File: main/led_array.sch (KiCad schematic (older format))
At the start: 220 parts

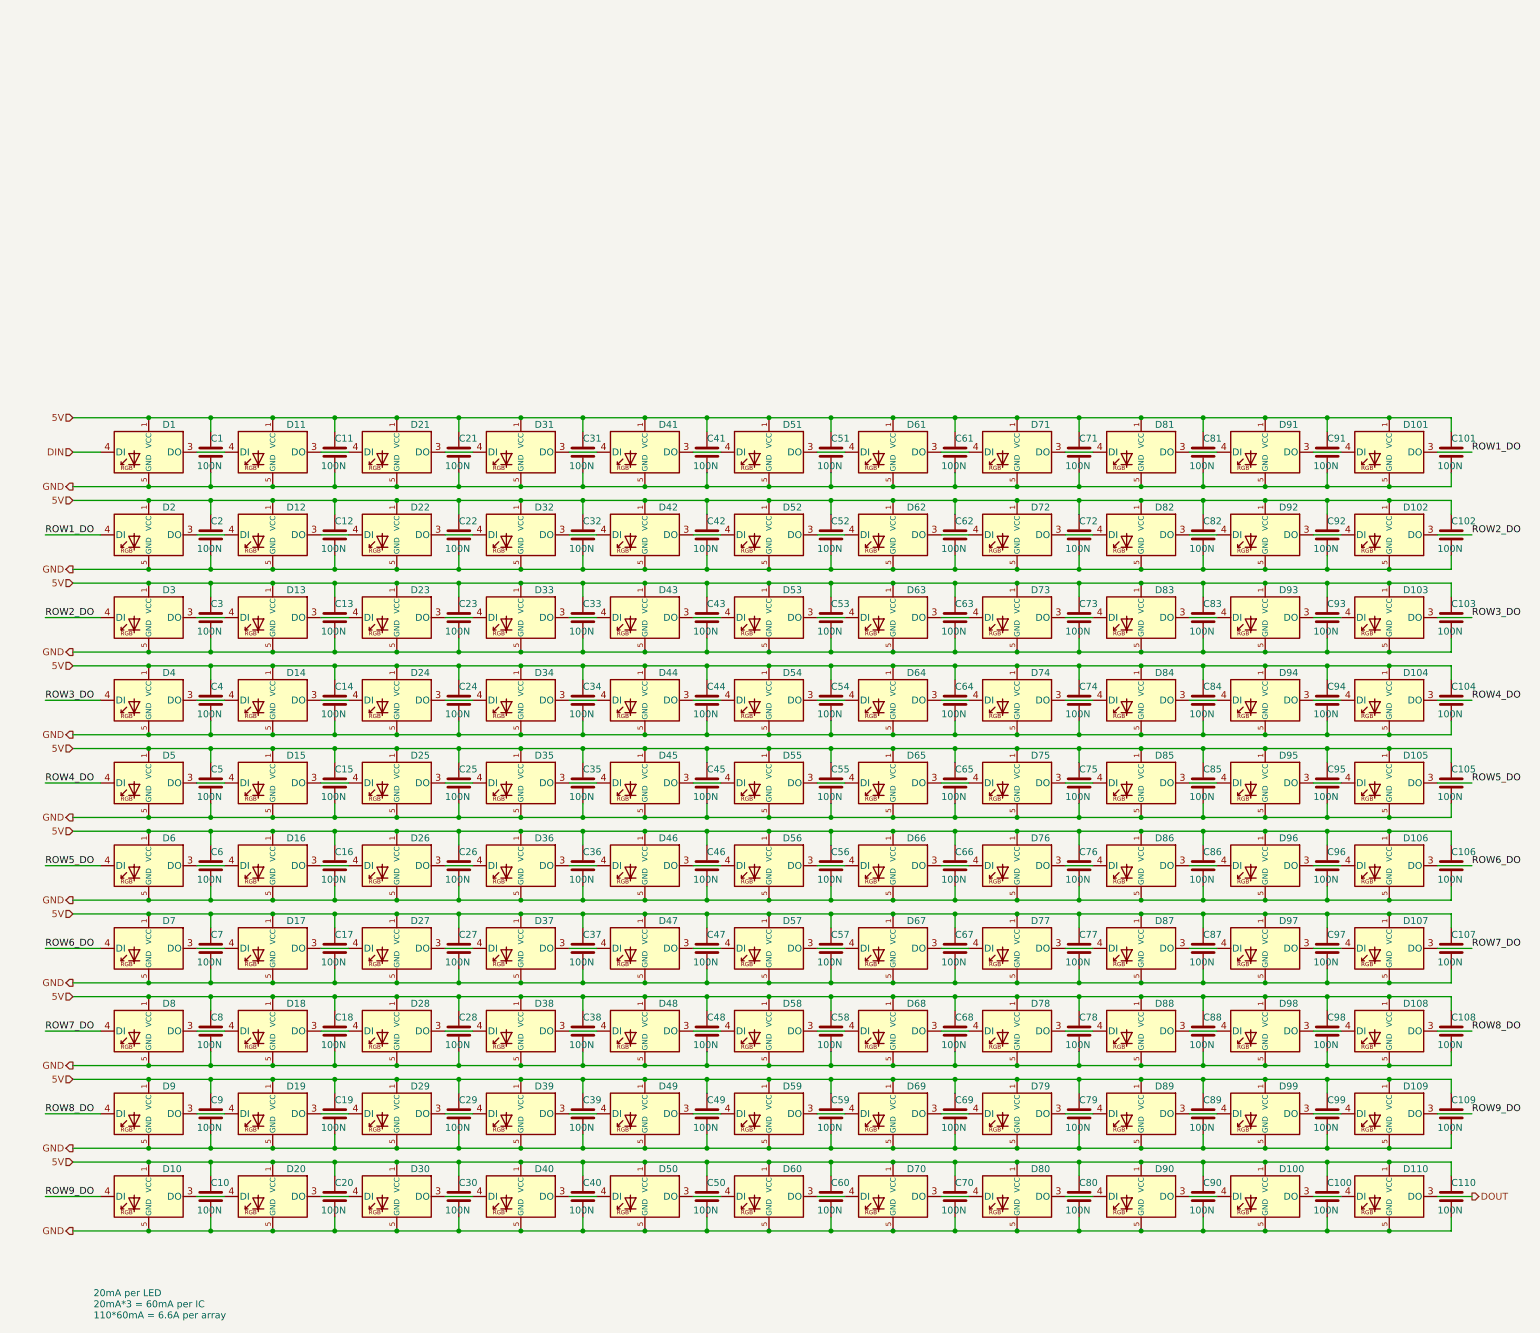
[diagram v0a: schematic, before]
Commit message: started layout to see if practical
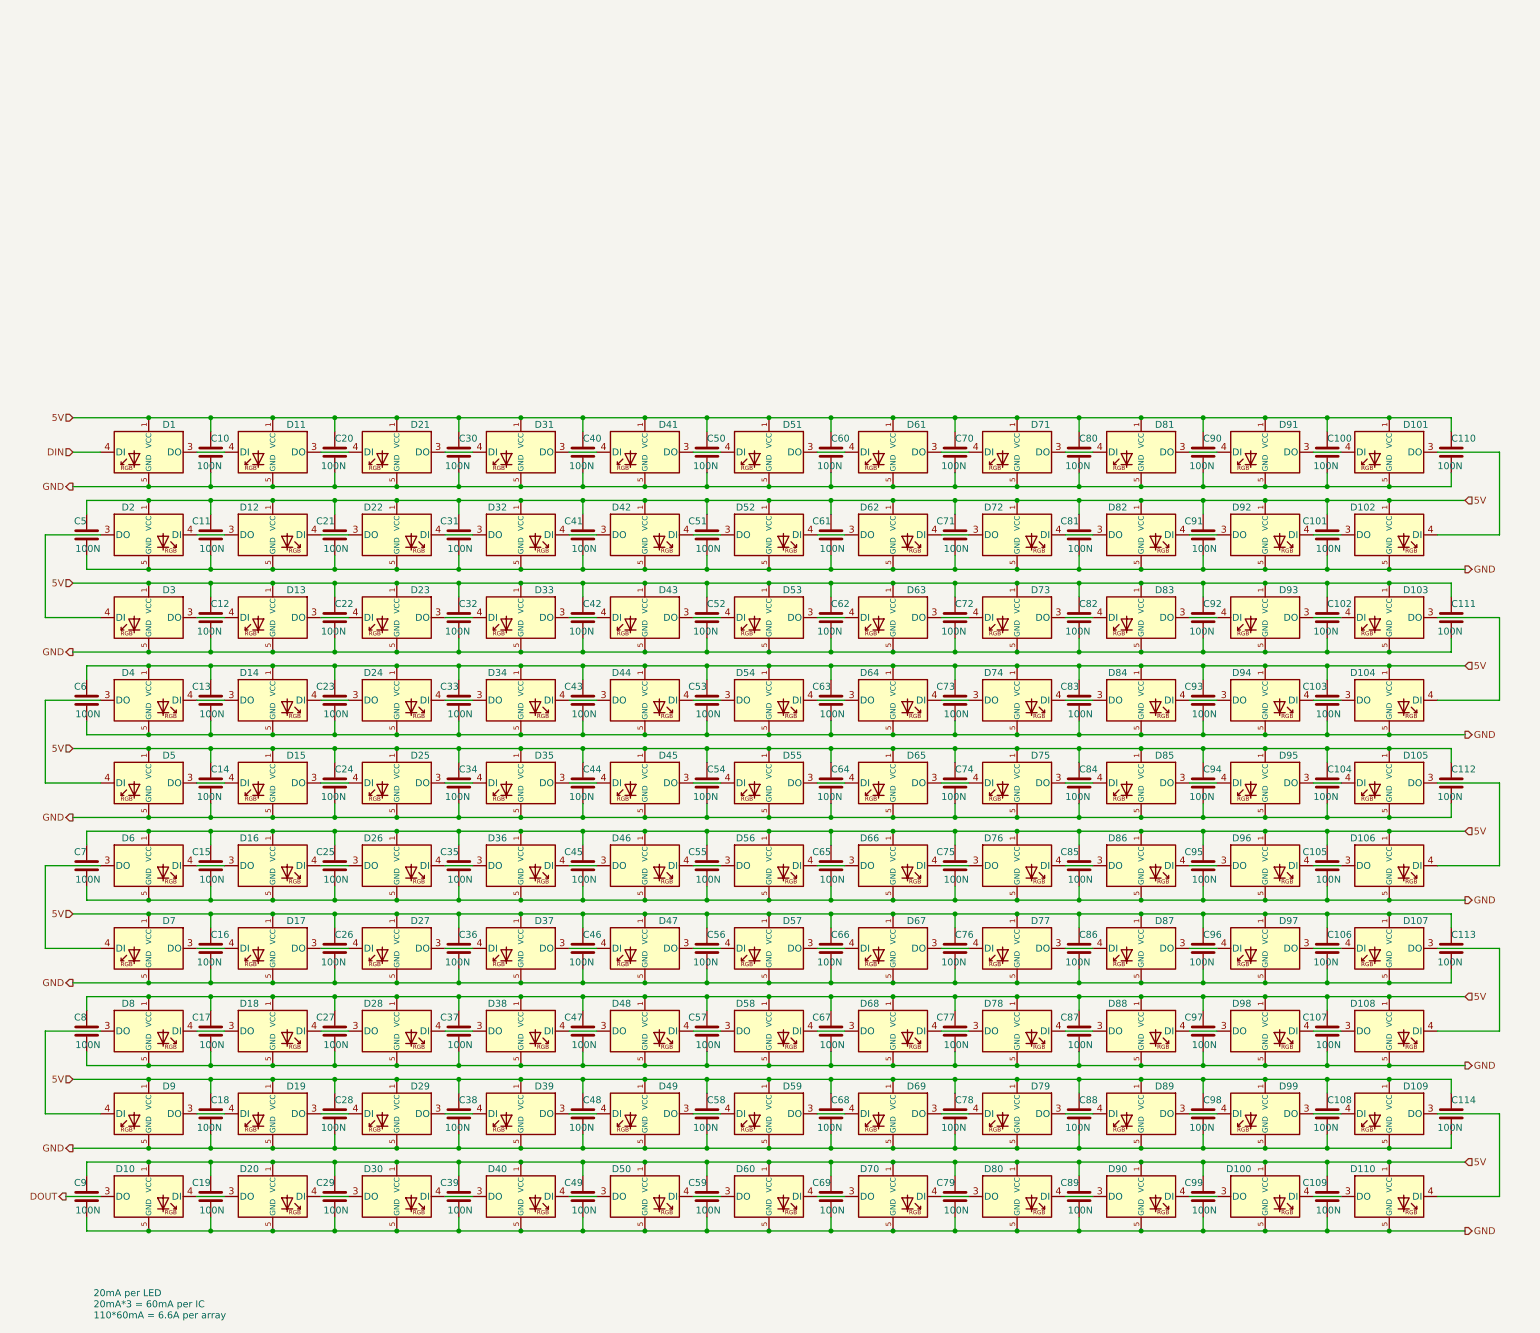
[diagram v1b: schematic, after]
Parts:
- renumbered C1 to C10, C91 to C100, C2 to C101, C93 to C102, C4 to C103, C95 to C104, C6 to C105, C97 to C106, C8 to C107, C99 to C108, C10 to C109, C92 to C11, C101 to C110, C103 to C111, C105 to C112, C107 to C113, C109 to C114, C3 to C12, C94 to C13, C5 to C14, C96 to C15, C7 to C16, C98 to C17, C9 to C18, C100 to C19, C11 to C20, C82 to C21, C13 to C22, C84 to C23, C15 to C24, C86 to C25, C17 to C26, C88 to C27, C19 to C28, C90 to C29, C21 to C30, C72 to C31, C23 to C32, C74 to C33, C25 to C34, C76 to C35, C27 to C36, C78 to C37, C29 to C38, C80 to C39, C31 to C40, C62 to C41, C33 to C42, C64 to C43, C35 to C44, C66 to C45, C37 to C46, C68 to C47, C39 to C48, C70 to C49, C102 to C5, C41 to C50, C52 to C51, C43 to C52, C54 to C53, C45 to C54, C56 to C55, C47 to C56, C58 to C57, C49 to C58, C60 to C59, C104 to C6, C51 to C60, C42 to C61, C53 to C62, C44 to C63, C55 to C64, C46 to C65, C57 to C66, C48 to C67, C59 to C68, C50 to C69, C106 to C7, C61 to C70, C32 to C71, C63 to C72, C34 to C73, C65 to C74, C36 to C75, C67 to C76, C38 to C77, C69 to C78, C40 to C79, C108 to C8, C71 to C80, C22 to C81, C73 to C82, C24 to C83, C75 to C84, C26 to C85, C77 to C86, C28 to C87, C79 to C88, C30 to C89, C110 to C9, C81 to C90, C12 to C91, C83 to C92, C14 to C93, C85 to C94, C16 to C95, C87 to C96, C18 to C97, C89 to C98, C20 to C99, D110 to D10, D20 to D100, D2 to D102, D4 to D104, D6 to D106, D8 to D108, D10 to D110, D92 to D12, D94 to D14, D96 to D16, D98 to D18, D102 to D2, D100 to D20, D82 to D22, D84 to D24, D86 to D26, D88 to D28, D90 to D30, D72 to D32, D74 to D34, D76 to D36, D78 to D38, D104 to D4, D80 to D40, D62 to D42, D64 to D44, D66 to D46, D68 to D48, D70 to D50, D106 to D6, D42 to D62, D44 to D64, D46 to D66, D48 to D68, D50 to D70, D32 to D72, D34 to D74, D36 to D76, D38 to D78, D108 to D8, D40 to D80, D22 to D82, D24 to D84, D26 to D86, D28 to D88, D30 to D90, D12 to D92, D14 to D94, D16 to D96, D18 to D98
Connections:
- net ROW1_DO: no longer names the net of D101.3 (DO), D102.4 (DI), D102.6 (BIN)
- net ROW2_DO: no longer names the net of D2.3 (DO), D3.4 (DI), D3.6 (BIN)
- net ROW3_DO: no longer names the net of D103.3 (DO), D104.4 (DI), D104.6 (BIN)
- net ROW4_DO: no longer names the net of D4.3 (DO), D5.4 (DI), D5.6 (BIN)
- net ROW5_DO: no longer names the net of D105.3 (DO), D106.4 (DI), D106.6 (BIN)
- net ROW6_DO: no longer names the net of D6.3 (DO), D7.4 (DI), D7.6 (BIN)
- net ROW7_DO: no longer names the net of D107.3 (DO), D108.4 (DI), D108.6 (BIN)
- net ROW8_DO: no longer names the net of D8.3 (DO), D9.4 (DI), D9.6 (BIN)
- net ROW9_DO: no longer names the net of D109.3 (DO), D110.4 (DI), D110.6 (BIN)
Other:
- moved on the sheet: C101, C103, C105, C107, C109, C11, C13, C15, C17, C19, C21, C23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

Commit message: most components
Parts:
- C10, C100, C101, C102, C103, C104, C105, C106, C107, C108, C109, C11, C110, C111, C112, C113, C114, C12, C13, C14, C15, C16, C17, C18, C19, C20, C21, C22, C23, C24, C25, C26, C27, C28, C29, C30, C31, C32, C33, C34, C35, C36, C37, C38, C39, C40, C41, C42, C43, C44, C45, C46, C47, C48, C49, C5, C50, C51, C52, C53, C54, C55, C56, C57, C58, C59, C6, C60, C61, C62, C63, C64, C65, C66, C67, C68, C69, C7, C70, C71, C72, C73, C74, C75, C76, C77, C78, C79, C8, C80, C81, C82, C83, C84, C85, C86, C87, C88, C89, C9, C90, C91, C92, C93, C94, C95, C96, C97, C98, C99: footprint Capacitor_SMD:C_0603_1608Metric -> Capacitor_SMD:C_0402_1005Metric
- D1, D10, D100, D101, D102, D103, D104, D105, D106, D107, D108, D109, D11, D110, D12, D13, D14, D15, D16, D17, D18, D19, D2, D20, D21, D22, D23, D24, D25, D26, D27, D28, D29, D3, D30, D31, D32, D33, D34, D35, D36, D37, D38, D39, D4, D40, D41, D42, D43, D44, D45, D46, D47, D48, D49, D5, D50, D51, D52, D53, D54, D55, D56, D57, D58, D59, D6, D60, D61, D62, D63, D64, D65, D66, D67, D68, D69, D7, D70, D71, D72, D73, D74, D75, D76, D77, D78, D79, D8, D80, D81, D82, D83, D84, D85, D86, D87, D88, D89, D9, D90, D91, D92, D93, D94, D95, D96, D97, D98, D99: footprint LED_SMD:LED_WS2812_PLCC6_5.0x5.0mm_P1.6mm -> william_led:WS2813-Mini-3.5mm_x_3.5mm

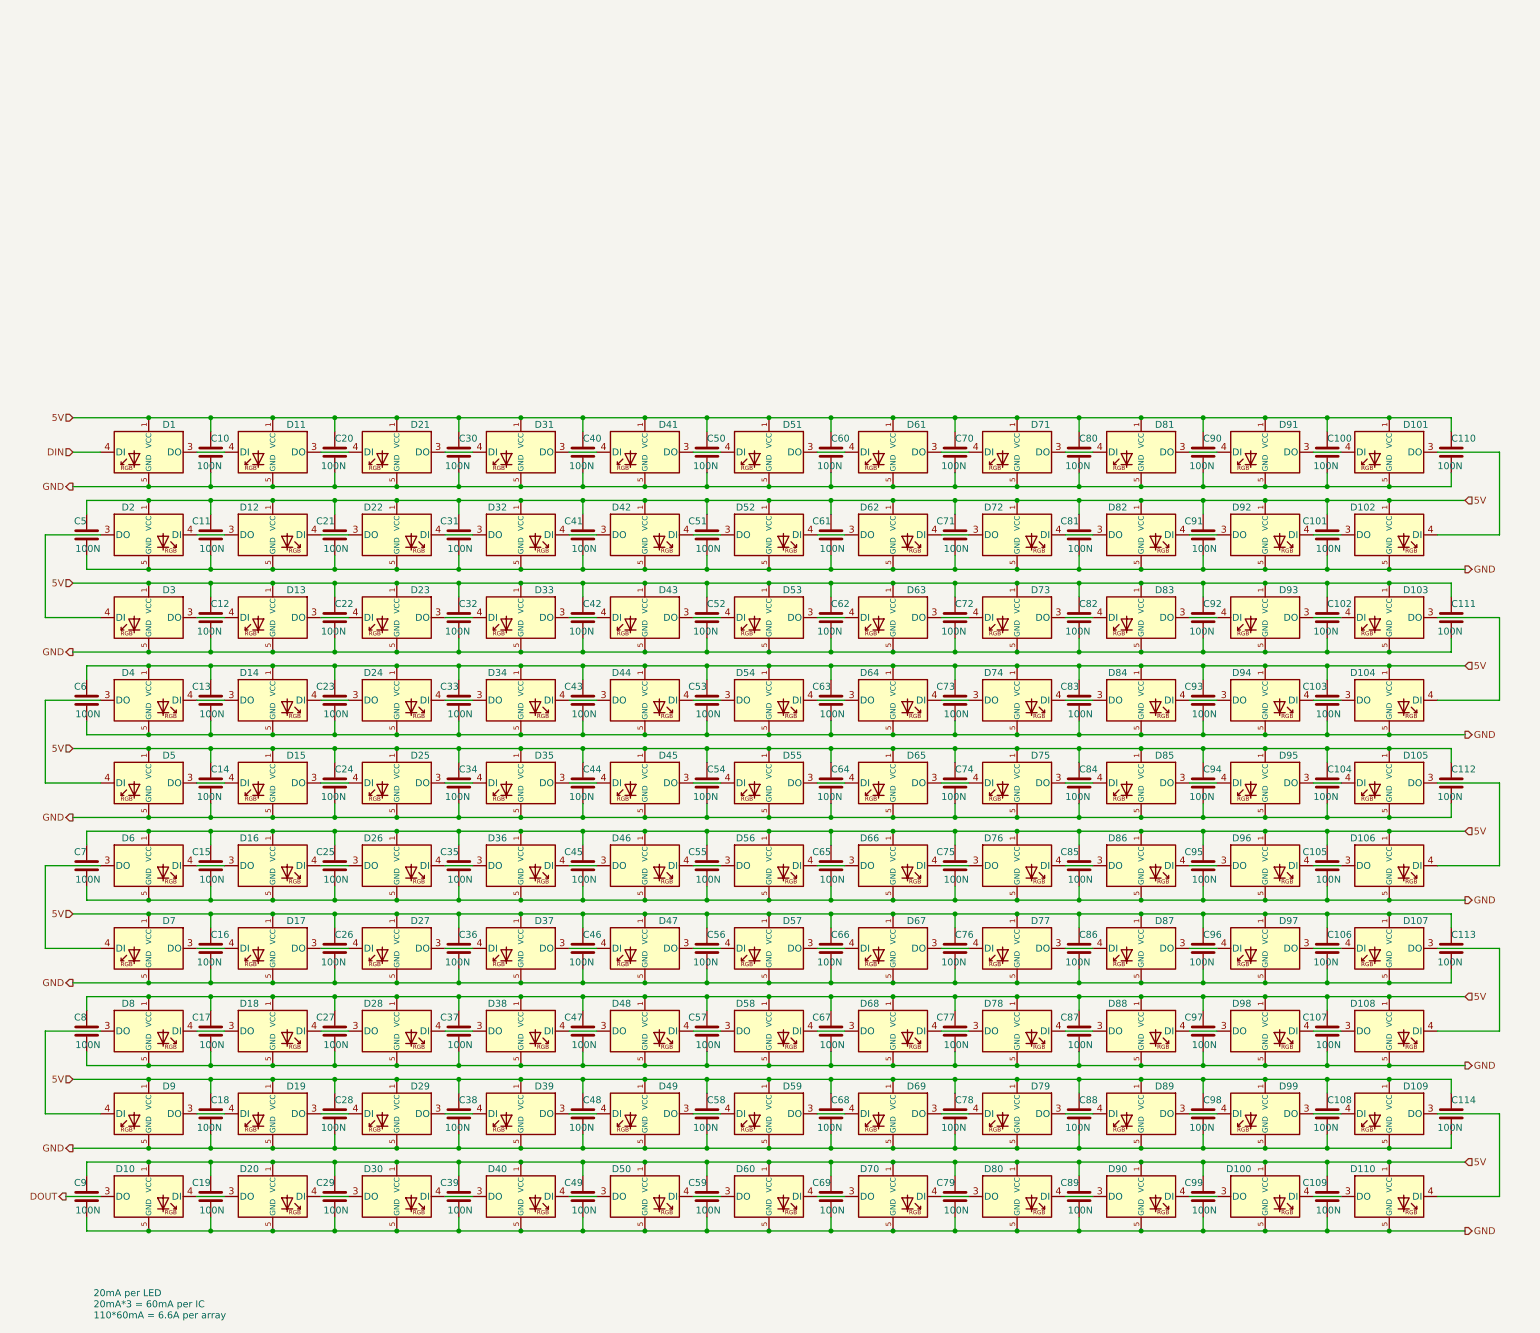
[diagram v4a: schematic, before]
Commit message: made spacer layer, replaces Ws2813 with WS2812, fixed fabrication for v0.0.0, now v0.1.0
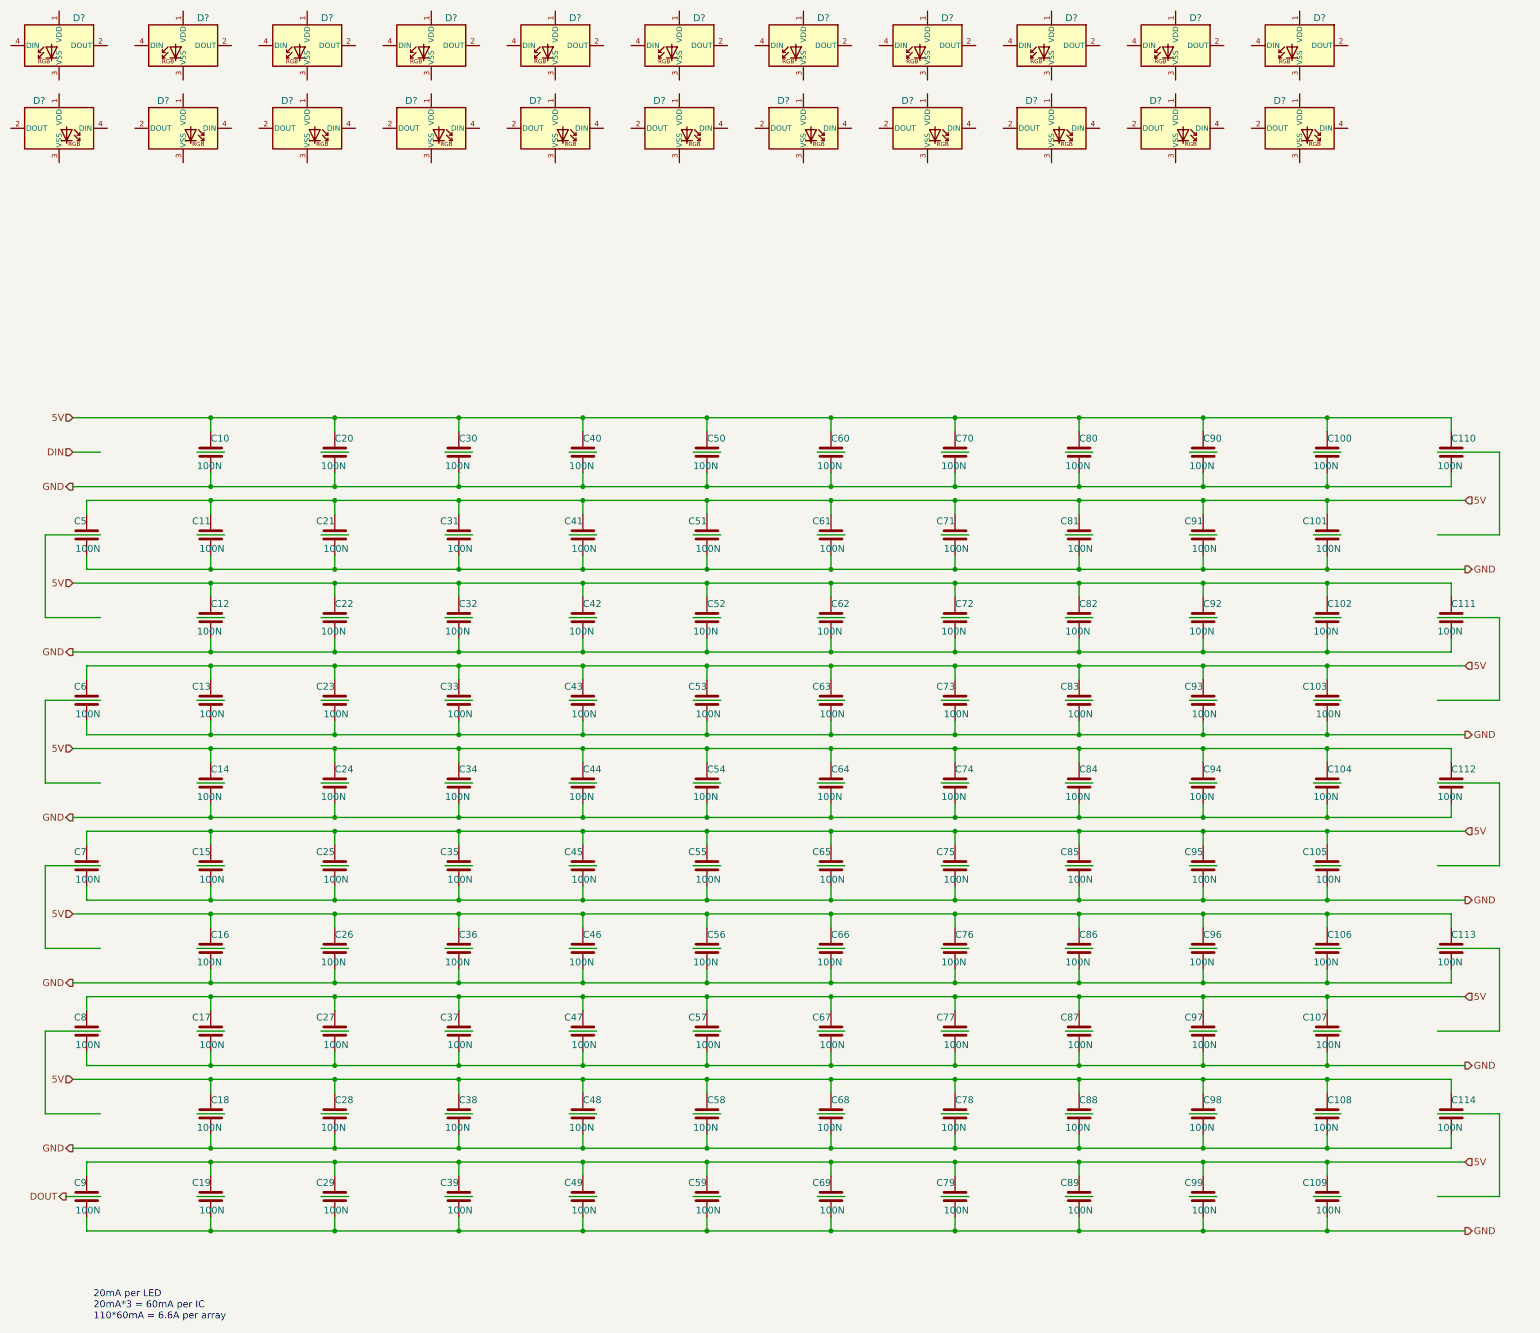
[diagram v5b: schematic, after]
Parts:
- removed D1, D10, D100, D101, D102, D103, D104, D105, D106, D107, D108, D109, D11, D110, D12, D13, D14, D15, D16, D17, D18, D19, D2, D20, D21, D22, D23, D24, D25, D26, D27, D28, D29, D3, D30, D31, D32, D33, D34, D35, D36, D37, D38, D39, D4, D40, D41, D42, D43, D44, D45, D46, D47, D48, D49, D5, D50, D51, D52, D53, D54, D55, D56, D57, D58, D59, D6, D60, D61, D62, D63, D64, D65, D66, D67, D68, D69, D7, D70, D71, D72, D73, D74, D75, D76, D77, D78, D79, D8, D80, D81, D82, D83, D84, D85, D86, D87, D88, D89, D9, D90, D91, D92, D93, D94, D95, D96, D97, D98, D99: WS2813-Mini, william_led:WS2813-Mini-3.5mm_x_3.5mm, symbol william_led:WS2813-Mini
- added D? (x22): WS2813-Mini, william_led:WS2813-Mini-3.5mm_x_3.5mm, symbol william_led:WS2812B-MINI
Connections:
- wire segments 789 -> 569
